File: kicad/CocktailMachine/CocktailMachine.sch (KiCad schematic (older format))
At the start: 40 parts

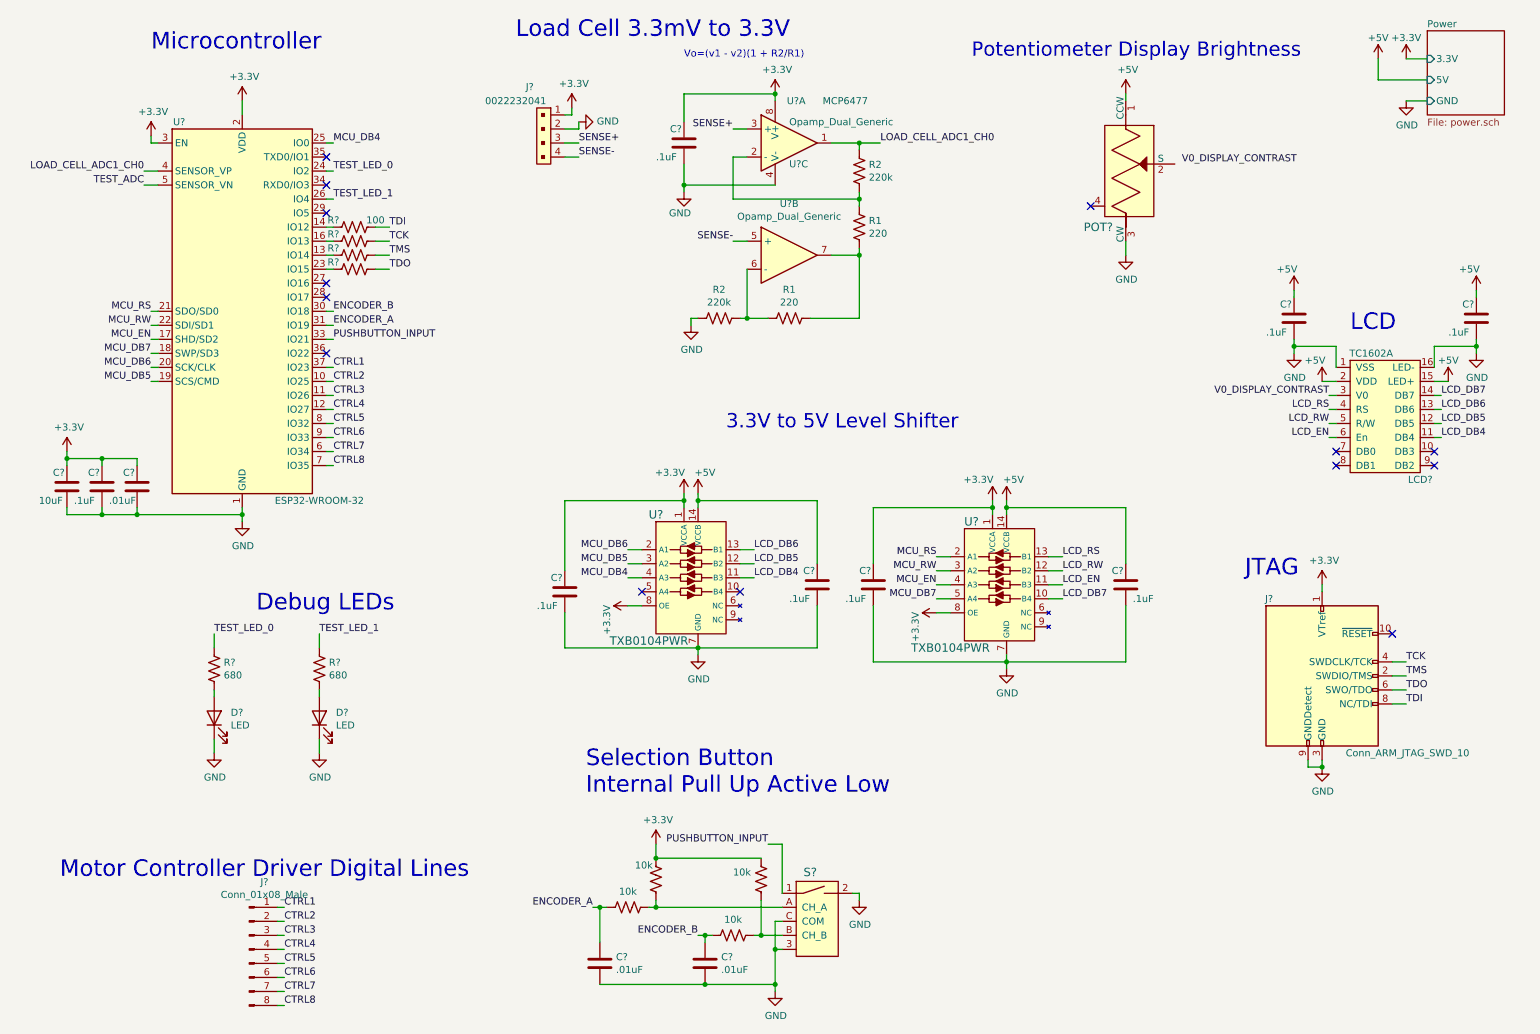
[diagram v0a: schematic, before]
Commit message: Generate footprints and netlist. Begin Layout.
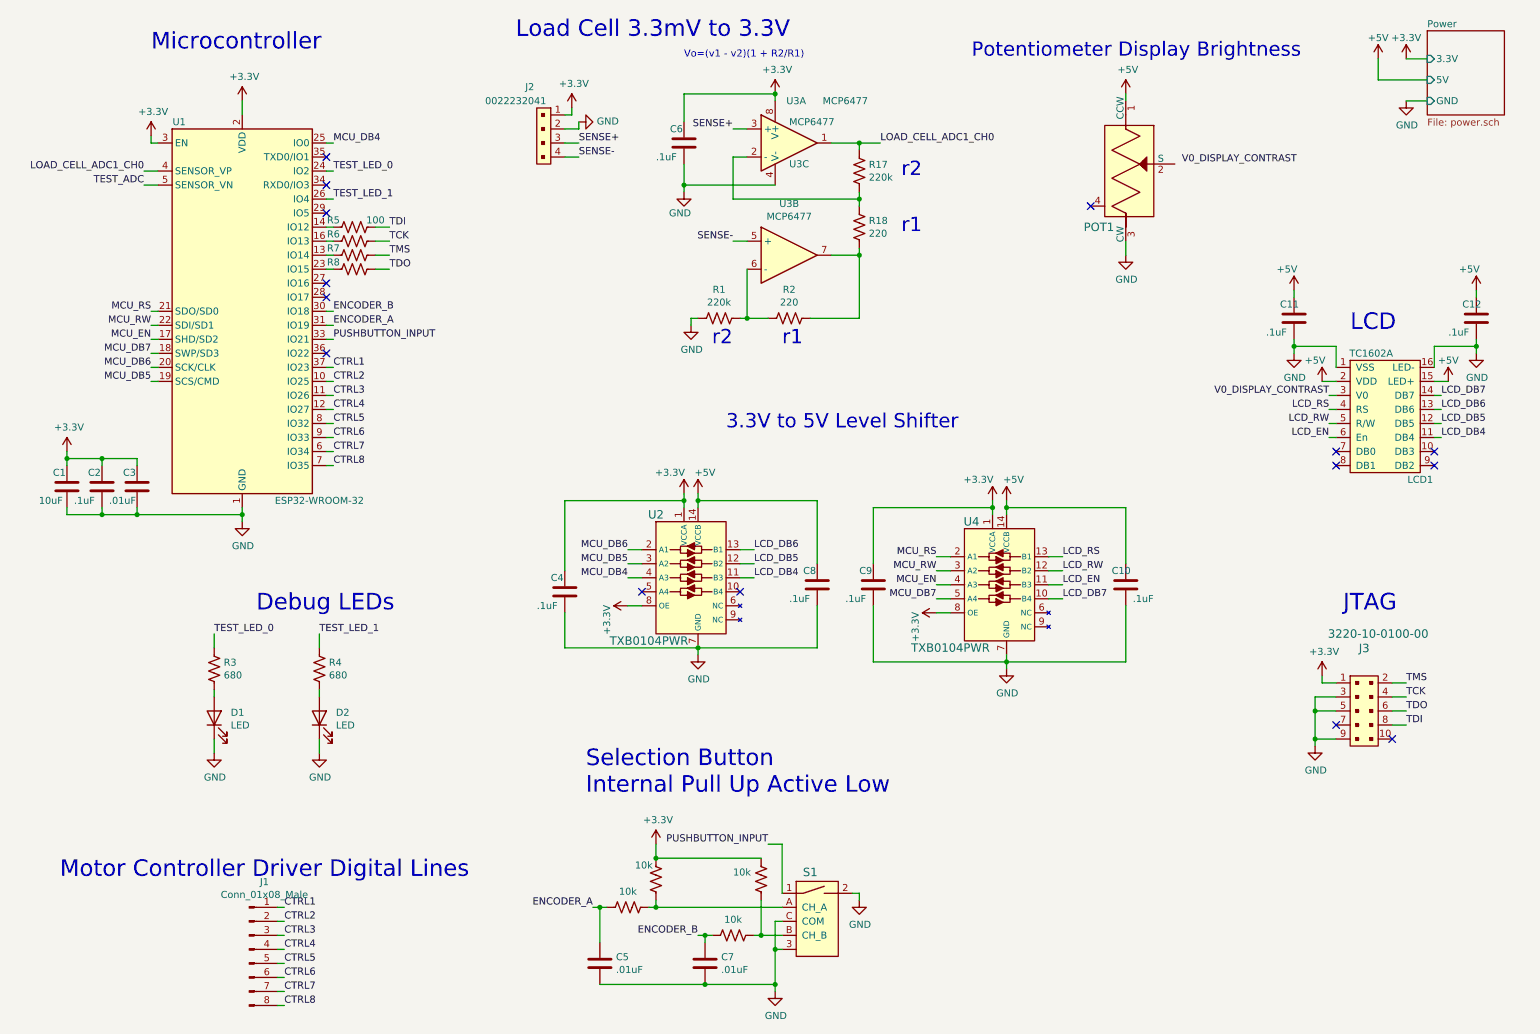
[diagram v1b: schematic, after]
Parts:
- removed J?: Conn_ARM_JTAG_SWD_10, symbol Connector:Conn_ARM_JTAG_SWD_10
- added J3: 3220-10-0100-00, digikey-footprints:PinHeader_2x5_P1.27mm_Drill.7mm, symbol dk_Rectangular-Connectors-Headers-Male-Pins:3220-10-0100-00
- C1, C10, C11, C12, C2, C3, C4, C5, C6, C7, C8, C9: renamed from C?; footprint (none) -> Capacitor_SMD:C_0603_1608Metric
- D1, D2: renamed from D?; footprint (none) -> LED_THT:LED_D3.0mm
- J1: renamed from J?; footprint (none) -> Connector_PinHeader_2.54mm:PinHeader_1x08_P2.54mm_Vertical
- LCD1: renamed from LCD?; footprint (none) -> CocktailMachine:TC1062A
- R1, R17: renamed from R2; footprint Resistor_THT:R_Axial_DIN0204_L3.6mm_D1.6mm_P2.54mm_Vertical -> Resistor_SMD:R_0603_1608Metric
- R10, R11, R12, R3, R4, R9: renamed from R?; footprint Resistor_THT:R_Axial_DIN0204_L3.6mm_D1.6mm_P2.54mm_Vertical -> Resistor_SMD:R_0603_1608Metric
- R18, R2: renamed from R1; footprint Resistor_THT:R_Axial_DIN0204_L3.6mm_D1.6mm_P2.54mm_Vertical -> Resistor_SMD:R_0603_1608Metric
- R5, R6, R7, R8: renamed from R?; footprint (none) -> Resistor_SMD:R_0603_1608Metric
- U3: renamed from U?; footprint (none) -> CocktailMachine:MCP6477-MSOP
- U3: renamed from U?; value Opamp_Dual_Generic -> MCP6477; footprint (none) -> CocktailMachine:MCP6477-MSOP
- gave numbers to parts that had none: 6
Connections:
- net +3V3: now also J3.1
- net GND: now also J3.3, J3.5, J3.9
- net TCK: now also J3.4
- net TDI: now also J3.8
- net TDO: now also J3.6
- net TMS: now also J3.2
- no-connect marks 14 -> 15
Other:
- note added: "r1\n"
- note added: "r2"

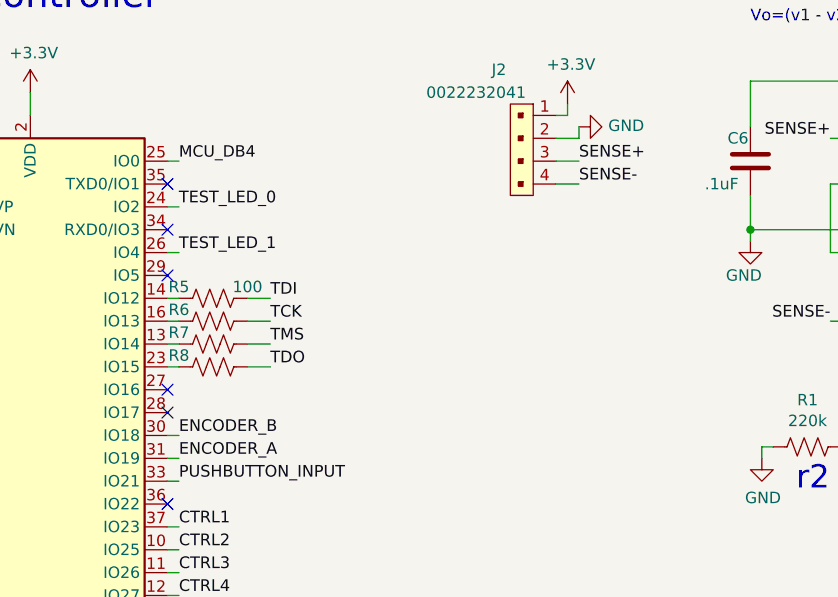
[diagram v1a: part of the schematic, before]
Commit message: Add extra pin headers before layout
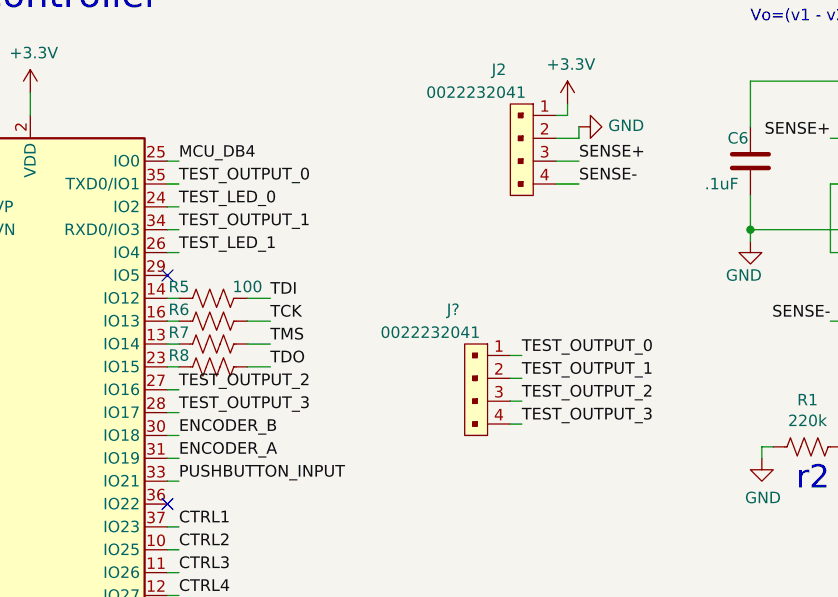
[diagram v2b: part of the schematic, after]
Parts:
- added J?: 0022232041, digikey-footprints:PinHeader_1x4_P2.54mm_Drill1.02mm, symbol dk_Rectangular-Connectors-Headers-Male-Pins:0022232041
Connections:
- net TEST_OUTPUT_2: now reaches U1.27 (IO16)
- net TEST_OUTPUT_2: now also J?.3
- net TEST_OUTPUT_3: now reaches U1.28 (IO17)
- net TEST_OUTPUT_3: now also J?.4
- net TEST_OUTPUT_1: now reaches U1.34 (RXD0/IO3)
- net TEST_OUTPUT_1: now also J?.2
- net TEST_OUTPUT_0: now reaches U1.35 (TXD0/IO1)
- net TEST_OUTPUT_0: now also J?.1
- no-connect marks 15 -> 11
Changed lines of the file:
@@
 	9600 2900 9600 2950
 Connection ~ 9600 2950
-NoConn ~ 2700 1600
-NoConn ~ 2700 1800
 NoConn ~ 2700 2000
-NoConn ~ 2700 2500
-NoConn ~ 2700 2600
 NoConn ~ 2700 3000
 Wire Wire Line
@@
 Text Notes 5450 2950 0    102  ~ 0
 r2
+$Comp
+L dk_Rectangular-Connectors-Headers-Male-Pins:0022232041 J?
+U 1 1 61AF6D3E
+P 4100 2350
+F 0 "J?" V 3900 2200 50  0000 C CNN
+F 1 "0022232041" V 4000 2100 50  0000 C CNN
+F 2 "digikey-footprints:PinHeader_1x4_P2.54mm_Drill1.02mm" H 4300 2550 60  0001 L CNN
+F 3 "https://www.molex.com/pdm_docs/sd/022232041_sd.pdf" H 4300 2650 60  0001 L CNN
+F 4 "WM4202-ND" H 4300 2750 60  0001 L CNN "Digi-Key_PN"
+F 5 "0022232041" H 4300 2850 60  0001 L CNN "MPN"
+F 6 "Connectors, Interconnects" H 4300 2950 60  0001 L CNN "Category"
+F 7 "Rectangular Connectors - Headers, Male Pins" H 4300 3050 60  0001 L CNN "Family"
+F 8 "https://www.molex.com/pdm_docs/sd/022232041_sd.pdf" H 4300 3150 60  0001 L CNN "DK_Datasheet_Link"
+F 9 "/product-detail/en/molex/0022232041/WM4202-ND/26671" H 4300 3250 60  0001 L CNN "DK_Detail_Page"
+F 10 "CONN HEADER VERT 4POS 2.54MM" H 4300 3350 60  0001 L CNN "Description"
+F 11 "Molex" H 4300 3450 60  0001 L CNN "Manufacturer"
+F 12 "Active" H 4300 3550 60  0001 L CNN "Status"
+	1    4100 2350
+	0    1    1    0
+$EndComp
+Text Label 2750 2600 0    51   ~ 0
+TEST_OUTPUT_3
+Text Label 2750 2500 0    51   ~ 0
+TEST_OUTPUT_2
+Wire Wire Line
+	2750 2500 2700 2500
+Wire Wire Line
+	2700 2600 2750 2600
+Text Label 2750 1800 0    51   ~ 0
+TEST_OUTPUT_1
+Text Label 2750 1600 0    51   ~ 0
+TEST_OUTPUT_0
+Wire Wire Line
+	2750 1600 2700 1600
+Wire Wire Line
+	2700 1800 2750 1800
+Text Label 4250 2650 0    51   ~ 0
+TEST_OUTPUT_3
+Text Label 4250 2550 0    51   ~ 0
+TEST_OUTPUT_2
+Text Label 4250 2350 0    51   ~ 0
+TEST_OUTPUT_0
+Text Label 4250 2450 0    51   ~ 0
+TEST_OUTPUT_1
+Wire Wire Line
+	4250 2350 4200 2350
+Wire Wire Line
+	4250 2450 4200 2450
+Wire Wire Line
+	4250 2550 4200 2550
+Wire Wire Line
+	4200 2650 4250 2650
 $EndSCHEMATC
